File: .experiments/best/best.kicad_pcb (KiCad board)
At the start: 2 copper layers, 140 x 90 mm, 39 parts, among them J1 USB_C, J2 Output, J3 Debug, Q1 FS8205A, U1 USBLC6-2SC6, U2 BQ24072, U3 HY2113-KB5B, U4 MT3608, U5 AP2112K-3.3, U6 LN61CN3302MR-G

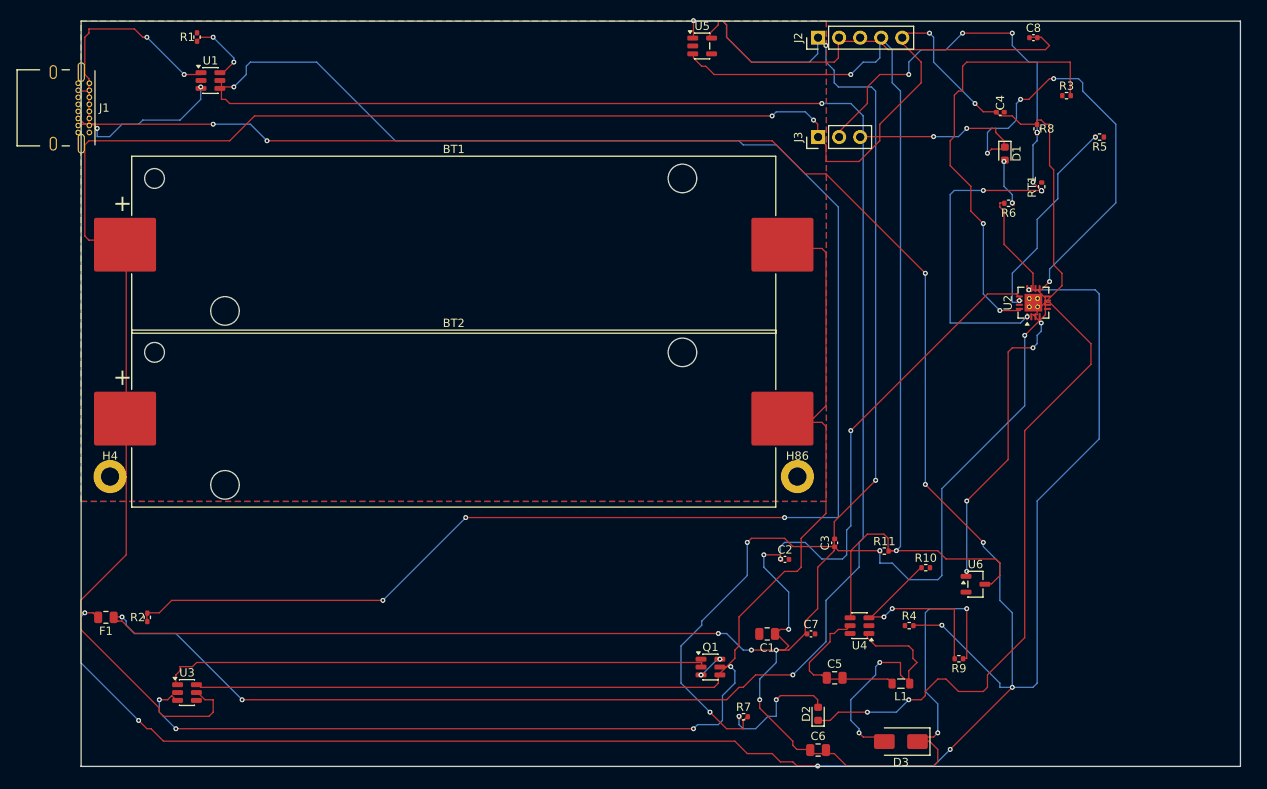
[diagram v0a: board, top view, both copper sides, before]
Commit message: Replace custom A*/RRR router with FreeRouting autorouter
- Created freerouting_runner.py: DSN export → FreeRouting CLI → SES import pipeline
- Subprocess-isolated pcbnew calls to avoid SwigPyObject stale-object bug
- dialog_confirmation_timeout: 0 suppresses blocking FreeRouting dialogs
- clear_traces() removes existing traces before each routing run
- Removed dead code: router.py, conflict.py, grid_builder.py, test_router_grid_behavior.py
- Updated config.py: replaced grid/A*/RRR keys with freerouting_jar/timeout/max_passes
- Updated pipeline.py RoutingEngine to call route_with_freerouting()
- Fixed ExperimentScore.compute() to use passed weights dict
- Updated autoexperiment.py mutations to placement-only params
- Added docs: architecture, scoring, freerouting-plan, footprint-layout
- Cleaned up stale files: LEARNINGS.md, ROUTING_IMPROVEMENTS.md, dashboard.png
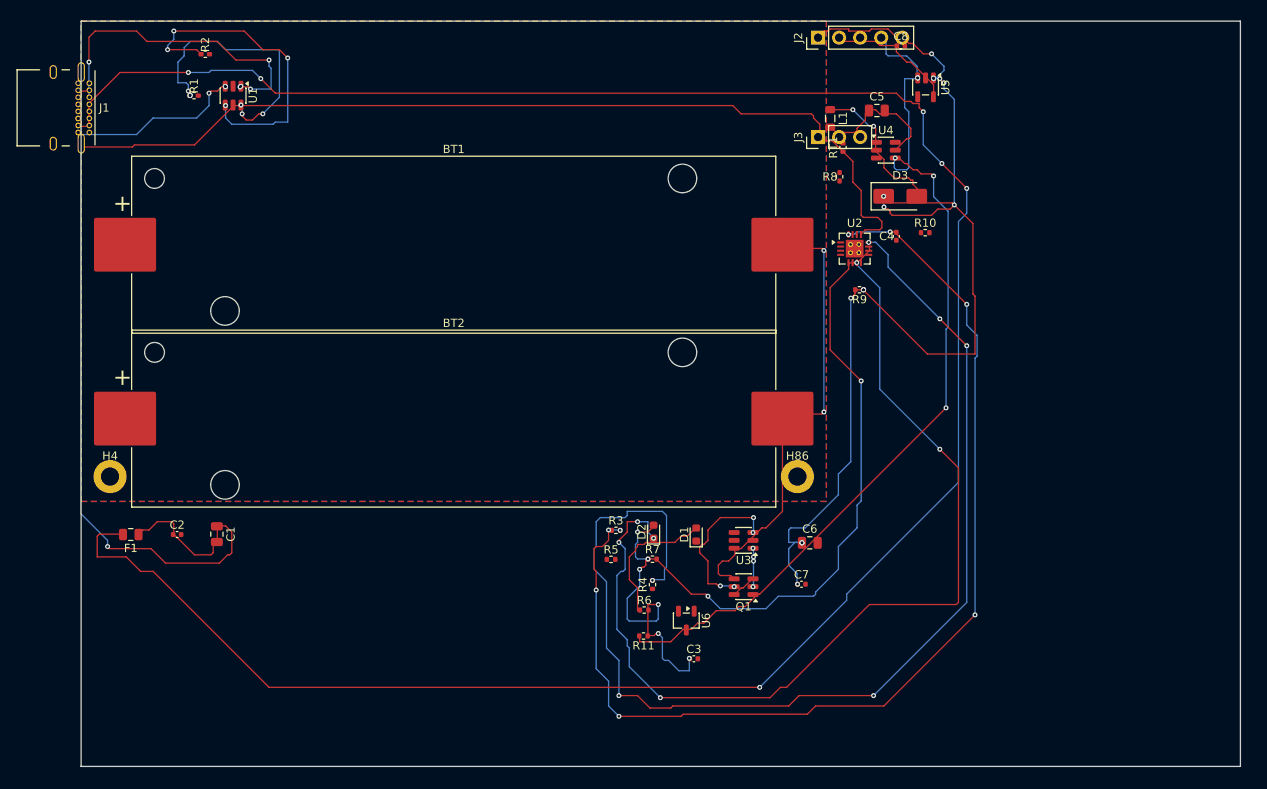
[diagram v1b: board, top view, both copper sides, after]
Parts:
- moved R5 78.0 mm to (64.0, 65.0), turned to 0 degrees
- moved R3 75.6 mm to (64.6, 61.5)
- moved C2 73.5 mm to (11.6, 62.0)
- moved U3 69.7 mm to (80.0, 62.7), turned to 180 degrees
- moved L1 68.8 mm to (90.5, 11.7), turned to -90 degrees
- moved C5 68.7 mm to (96.1, 10.8)
- moved R2 68.4 mm to (15.0, 4.00), turned to 0 degrees
- moved C1 67.5 mm to (16.4, 61.9), turned to -90 degrees
- moved R6 65.9 mm to (68.0, 71.1), turned to 0 degrees
- moved D3 65.8 mm to (98.9, 21.2), turned to 0 degrees
- moved D1 59.2 mm to (74.3, 62.0), turned to 90 degrees
- moved U4 57.5 mm to (97.2, 15.6), turned to 0 degrees
- moved R9 46.1 mm to (94.0, 32.4)
- moved R10 40.5 mm to (101.9, 25.5)
- moved U6 35.2 mm to (73.1, 72.4), turned to -90 degrees
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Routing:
- net /VBAT: track 296.8 -> 0.00 mm, vias 8 -> 0
- net /VBUS: track 393.0 -> 198.6 mm, vias 10 -> 2
- net Net-(R2-Pad1): track 210.3 -> 39.0 mm
- net /NTC_SENSE: track 86.6 -> 0.00 mm, vias 10 -> 0
- net /CELL_NEG: track 137.1 -> 55.6 mm, vias 0 -> 2
- net Net-(U2-ISET): track 52.6 -> 130.6 mm, vias 2 -> 8
- net /CHG_N: track 70.5 -> 0.00 mm, vias 6 -> 0
- net Net-(Q1B-G): track 82.0 -> 18.7 mm
- net Net-(Q1A-G): track 65.9 -> 4.50 mm, vias 0 -> 4
- net Net-(U2-ILIM): track 77.4 -> 137.9 mm, vias 2 -> 6
- net Net-(D2-K): track 77.9 -> 116.4 mm, vias 2 -> 6
- net /5V: track 174.3 -> 135.9 mm, vias 8 -> 14
- net /3V3: track 51.8 -> 15.8 mm
- net Net-(U4-FB): track 25.9 -> 0.00 mm, vias 2 -> 0
- net Net-(U2-TMR): track 25.1 -> 0.00 mm, vias 2 -> 0
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
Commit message: 28-round experiment (best 65.5), auto report+GIF generation, FreeRouting headless fix
- autoexperiment.py: fix JSON set serialization, auto-generate HTML report after run
- freerouting_runner.py: use --gui.enabled=false + -dct 0 for true headless mode
- 28-round experiment results (seed 701099954, best score 65.506)
- HTML report and progress GIF
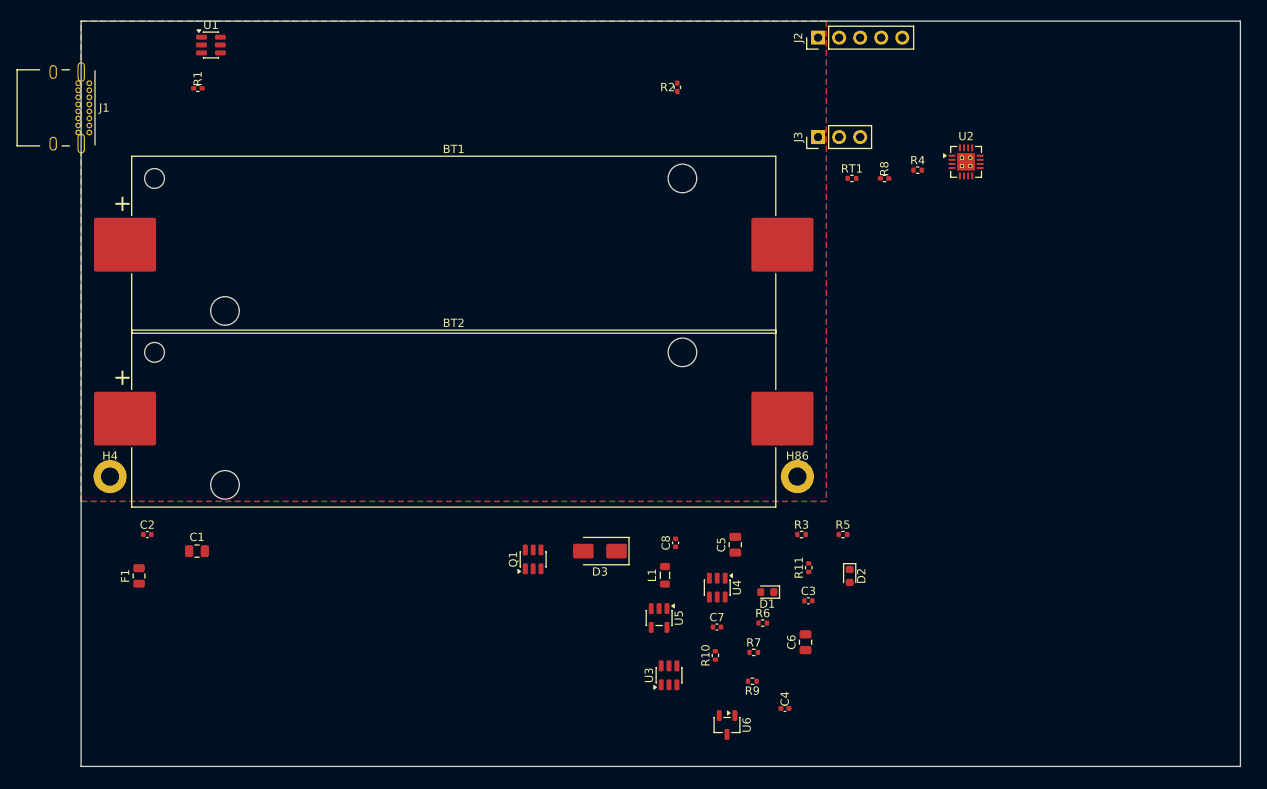
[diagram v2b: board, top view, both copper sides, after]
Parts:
- moved U5 71.7 mm to (69.8, 72.1)
- moved C8 65.9 mm to (71.8, 63.0), turned to 90 degrees
- moved R4 59.4 mm to (101.0, 18.0), turned to 0 degrees
- moved L1 58.7 mm to (70.5, 66.9), turned to 90 degrees
- moved C4 58.6 mm to (85.0, 83.0), turned to 0 degrees
- moved R2 57.1 mm to (72.0, 8.00), turned to 90 degrees
- moved R10 57.0 mm to (76.6, 76.6), turned to 90 degrees
- moved U4 56.6 mm to (76.8, 68.4), turned to -90 degrees
- moved D3 56.1 mm to (62.7, 64.0), turned to 180 degrees
- moved C5 55.2 mm to (79.0, 63.2), turned to 90 degrees
- moved R9 49.0 mm to (81.1, 79.7)
- moved R5 28.2 mm to (92.0, 62.0)
- moved Q1 25.6 mm to (54.6, 65.0), turned to 90 degrees
- moved D2 24.3 mm to (92.8, 67.0), turned to -90 degrees
- moved R3 22.4 mm to (87.0, 62.0)
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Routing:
- net Net-(F1-Pad2): track 287.9 -> 0.00 mm, vias 6 -> 0
- net /VBUS: track 198.6 -> 0.00 mm, vias 2 -> 0
- net Net-(U2-ILIM): track 137.9 -> 0.00 mm, vias 6 -> 0
- net /5V: track 135.9 -> 0.00 mm, vias 14 -> 0
- net Net-(U2-ISET): track 130.6 -> 0.00 mm, vias 8 -> 0
- net Net-(D2-K): track 116.4 -> 0.00 mm, vias 6 -> 0
- net /EN: track 107.7 -> 0.00 mm, vias 6 -> 0
- net /VSYS: track 100.9 -> 0.00 mm, vias 6 -> 0
- net /CELL_NEG: track 55.6 -> 0.00 mm, vias 2 -> 0
- net Net-(R2-Pad1): track 39.0 -> 0.00 mm, vias 4 -> 0
- net Net-(J1-CC1): track 38.2 -> 0.00 mm, vias 6 -> 0
- net Net-(R1-Pad1): track 32.4 -> 0.00 mm, vias 6 -> 0
- net Net-(J1-CC2): track 22.8 -> 0.00 mm, vias 4 -> 0
- net Net-(Q1B-G): track 18.7 -> 0.00 mm, vias 4 -> 0
- net Net-(D3-A): track 18.5 -> 0.00 mm, vias 2 -> 0
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
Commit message: Remove old Python autorouter, clean references, update docs
Deleted:
- simple_router.py, reroute_net.py, _apply_routing.py (old A*/RRR router)
- BUGFIX_PLAN.md, IMPROVEMENT_PLAN.md (old planning docs)
- freerouting-plan.md, dashboard-automation.md (completed migration docs)
- experiments_dashboard.png (stale artifact)

Cleaned:
- autoroute.py: removed dead --no-rrr flag
- diff_rounds.py: removed A* Expansions and RRR timing fields
- generate_report.py: removed RRR timing and a_star_expansions column
- plot_experiments.py: removed RRR bar from timing chart
- SKILL.md: removed old router references from observability section

Updated docs:
- next-steps.md: rewritten for current state (150-round run complete)
- monitoring-guide.md: fixed timing chart description
- CHANGELOG.md: documented cleanup

Also includes: FreeRouting migration code changes (types.py, pipeline.py,
freerouting_runner.py, adapter.py), 150-round experiment results, and
updated architecture/auto-trace/README docs from prior sessions.
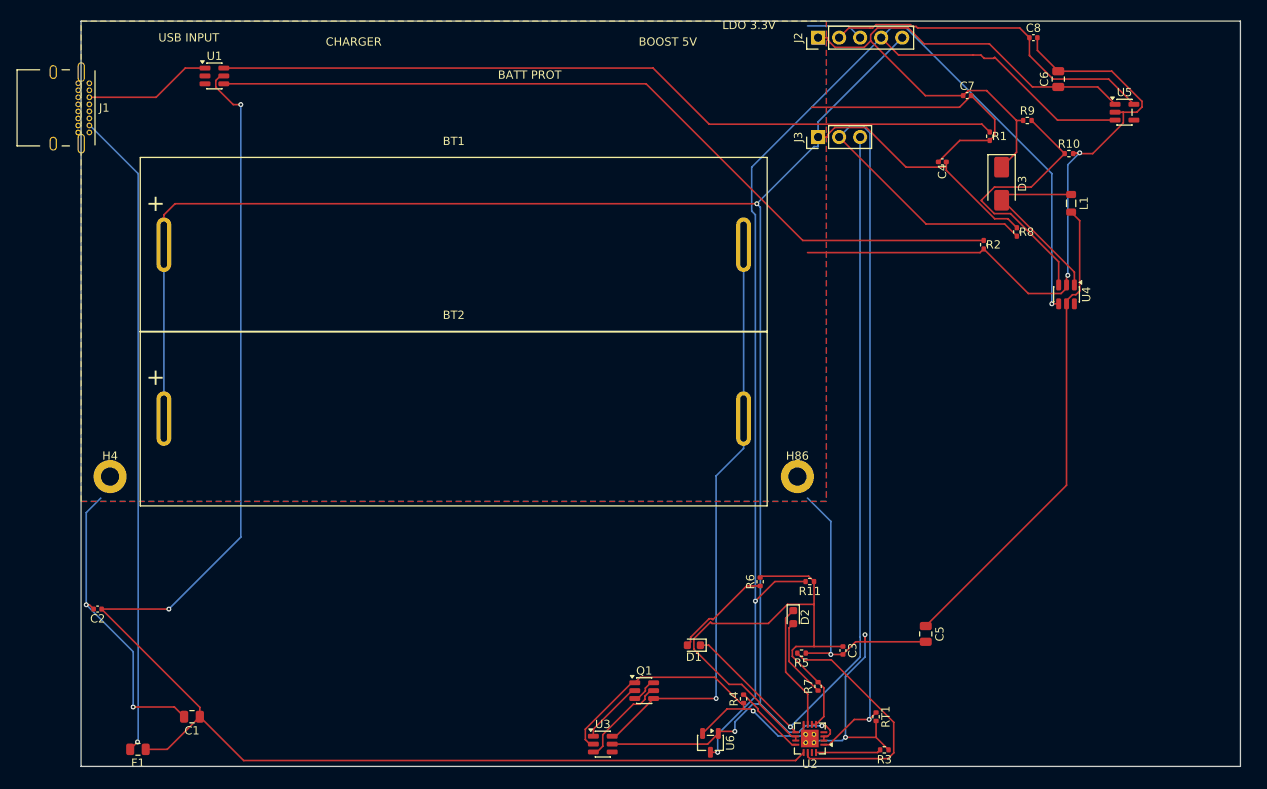
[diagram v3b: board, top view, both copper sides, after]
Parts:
- BT1, BT2: footprint Battery:BatteryHolder_Keystone_1042_1x18650 -> LLUPS:BatteryHolder_MYOUNG_BH-18650-A1AJ006
- moved R1 95.8 mm to (109.7, 13.9), turned to -90 degrees
- moved U5 83.0 mm to (126.0, 11.0), turned to 0 degrees
- moved R9 75.4 mm to (114.3, 12.0), turned to 0 degrees
- moved C8 74.8 mm to (115.0, 2.00), turned to 0 degrees
- moved C6 74.5 mm to (118.0, 7.00)
- moved R10 74.1 mm to (119.3, 16.0), turned to 0 degrees
- moved U2 72.1 mm to (88.0, 86.6), turned to 180 degrees
- moved C7 70.9 mm to (107.0, 9.00)
- moved C4 68.7 mm to (104.0, 17.0), turned to 180 degrees
- moved R4 67.2 mm to (80.0, 81.8), turned to 90 degrees
- moved L1 66.5 mm to (119.6, 22.0), turned to -90 degrees
- moved D3 65.7 mm to (111.2, 19.6), turned to -90 degrees
- moved RT1 65.1 mm to (96.0, 84.0), turned to -90 degrees
- moved U4 55.1 mm to (119.0, 33.0)
- moved R2 41.6 mm to (109.0, 27.0), turned to -90 degrees
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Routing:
- net GND: track 0.00 -> 266.0 mm, vias 0 -> 8
- net /VBAT: track 0.00 -> 248.3 mm, vias 0 -> 3
- net /EN: track 0.00 -> 180.2 mm, vias 0 -> 3
- net /VBUS: track 0.00 -> 180.1 mm, vias 0 -> 2
- net /NTC_SENSE: track 0.00 -> 109.7 mm, vias 0 -> 1
- net Net-(R2-Pad1): track 0.00 -> 99.6 mm
- net Net-(R1-Pad1): track 0.00 -> 95.7 mm
- net /CHG_N: track 0.00 -> 90.6 mm, vias 0 -> 1
- net Net-(F1-Pad2): track 0.00 -> 78.2 mm, vias 0 -> 1
- net /5V: track 0.00 -> 71.0 mm
- net /CELL_NEG: track 0.00 -> 70.6 mm, vias 0 -> 1
- net /VSYS: track 0.00 -> 67.3 mm
- net /VSYS_BOOST: track 0.00 -> 58.4 mm
- net /3V3: track 0.00 -> 41.5 mm
- net Net-(U4-FB): track 0.00 -> 33.3 mm
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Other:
- board text added: "BATT PROT"
- board text added: "BOOST 5V"
- board text added: "CHARGER"
- board text added: "LDO 3.3V"
- board text added: "USB INPUT"

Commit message: enforce pad containment for connectors/mounting holes
Remove all exceptions that allowed connector (J*) and mounting hole (H*)
pads to be placed outside PCB edge cuts:

- placement.py: Remove kind-based skip in _score_board_containment()
- placement.py: Remove kind and locked checks in _clamp_pads_to_board()
- adapter.py: Remove connector/mounting_hole from auto-lock (only battery)
- config.py: Remove exempt comment from pad_inset_margin_mm

150-round experiment: best score 89.91, 0 shorts all rounds,
board containment 99.5-100%.
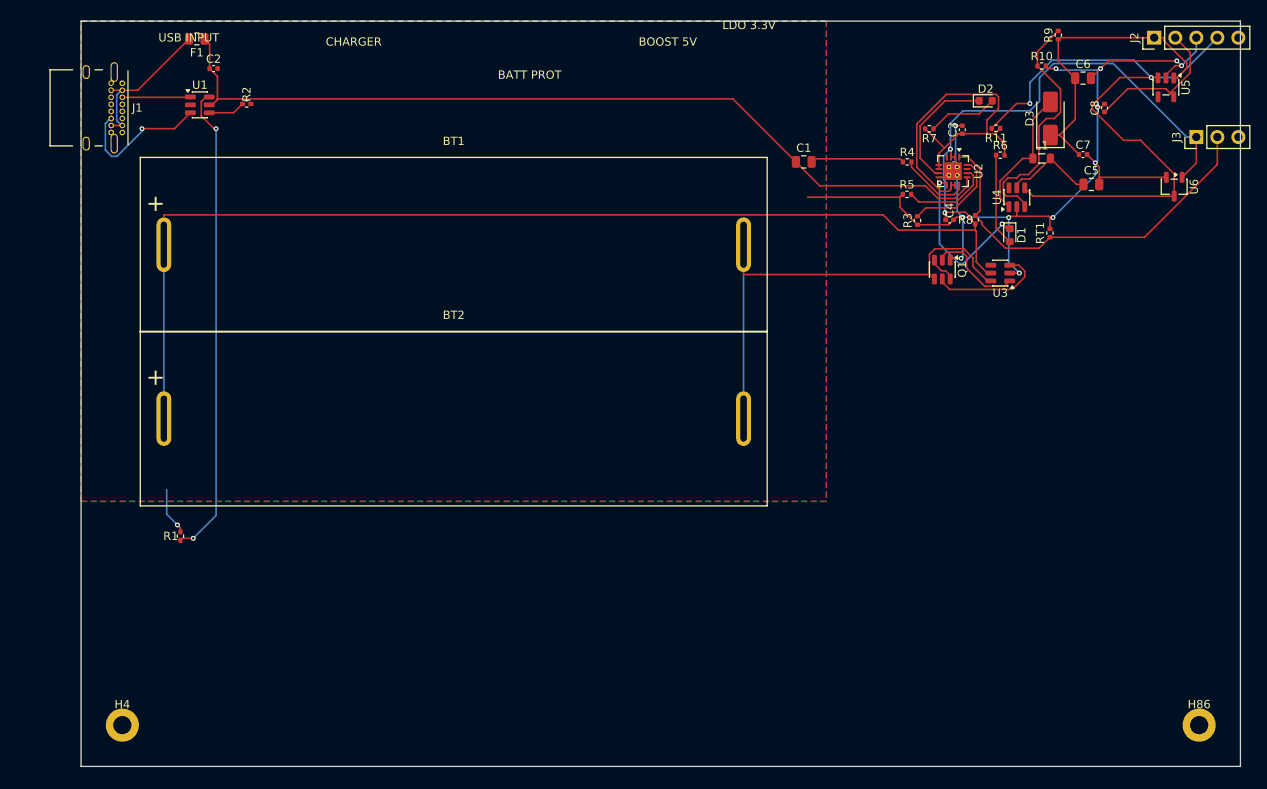
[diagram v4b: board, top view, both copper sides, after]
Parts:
- moved R1 109.0 mm to (12.0, 62.2), turned to 90 degrees
- moved C1 99.7 mm to (87.3, 17.0), turned to 0 degrees
- moved R2 90.6 mm to (20.0, 10.0), turned to 0 degrees
- moved U6 87.4 mm to (132.0, 20.0)
- moved F1 86.1 mm to (14.0, 2.15)
- moved U3 74.4 mm to (111.0, 30.4), turned to 180 degrees
- moved U2 70.7 mm to (105.3, 18.1), turned to -90 degrees
- moved R7 68.7 mm to (102.4, 13.0), turned to 180 degrees
- moved R4 67.8 mm to (99.8, 17.0), turned to 0 degrees
- moved C2 66.8 mm to (16.0, 5.73), turned to 0 degrees
- moved D2 66.5 mm to (109.2, 9.62), turned to 0 degrees
- moved C3 64.5 mm to (106.4, 13.1), turned to 90 degrees
- moved R3 64.0 mm to (101.0, 24.1), turned to 90 degrees
- moved D1 62.5 mm to (112.1, 25.8), turned to -90 degrees
- moved Q1 62.3 mm to (104.0, 30.0), turned to -90 degrees
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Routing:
- net GND: track 266.0 -> 142.2 mm, vias 8 -> 13
- net /EN: track 180.2 -> 79.1 mm, vias 3 -> 2
- net Net-(R2-Pad1): track 99.6 -> 4.45 mm
- net /VBUS: track 180.1 -> 106.4 mm, vias 2 -> 0
- net /CHG_N: track 90.6 -> 20.1 mm, vias 1 -> 2
- net /NTC_SENSE: track 109.7 -> 47.5 mm, vias 1 -> 0
- net Net-(F1-Pad2): track 78.2 -> 18.2 mm, vias 1 -> 0
- net /VBAT: track 248.3 -> 191.9 mm, vias 3 -> 2
- net /VSYS_BOOST: track 58.4 -> 11.1 mm
- net Net-(R1-Pad1): track 95.7 -> 57.6 mm, vias 0 -> 2
- net /5V: track 71.0 -> 37.3 mm
- net /3V3: track 41.5 -> 18.4 mm
- net /VSYS: track 67.3 -> 45.0 mm
- net Net-(U2-TMR): track 30.1 -> 10.8 mm
- net Net-(J1-CC2): track 0.00 -> 17.1 mm, vias 0 -> 1
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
